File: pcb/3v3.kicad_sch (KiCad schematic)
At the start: 6 parts, among them U3 AP3441SHE-7B

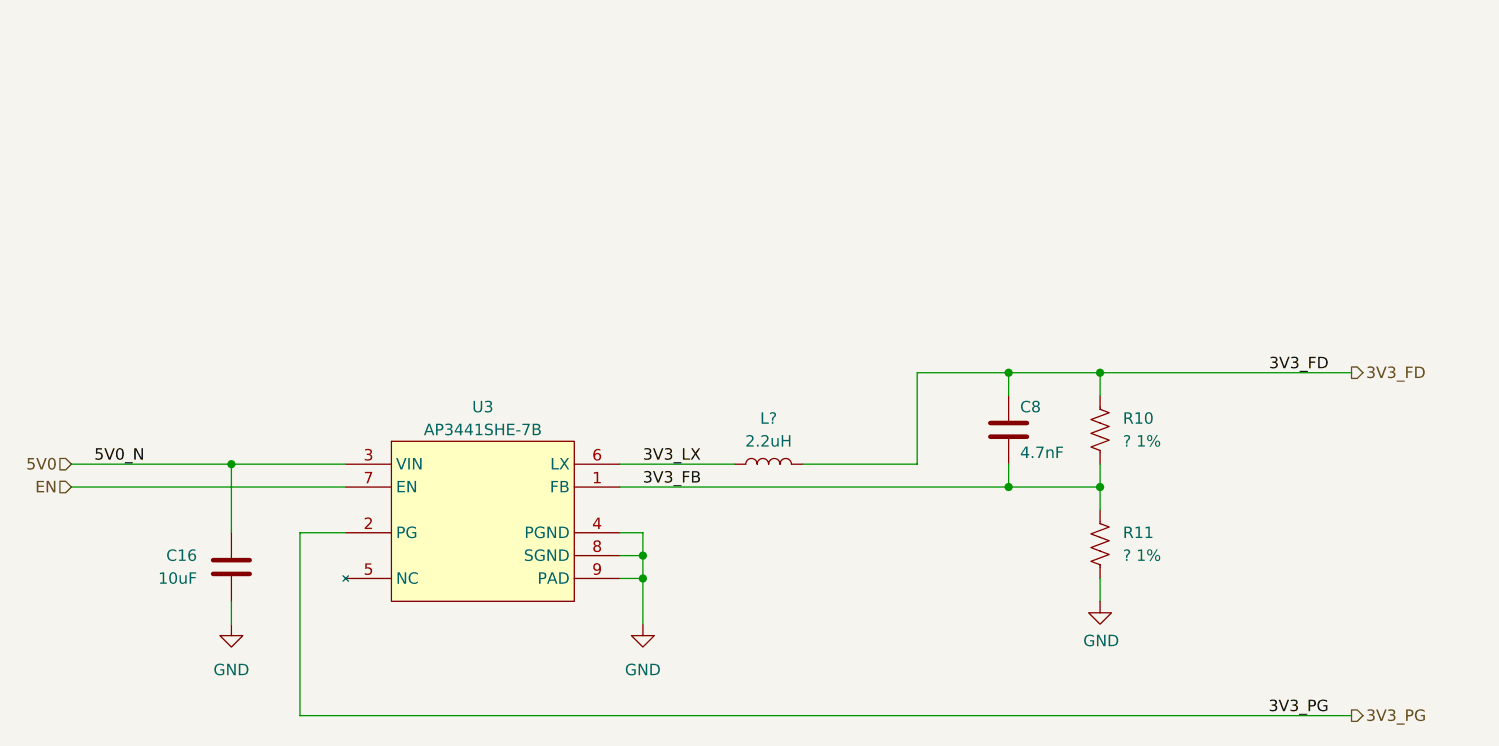
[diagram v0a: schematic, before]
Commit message: changes to power tree
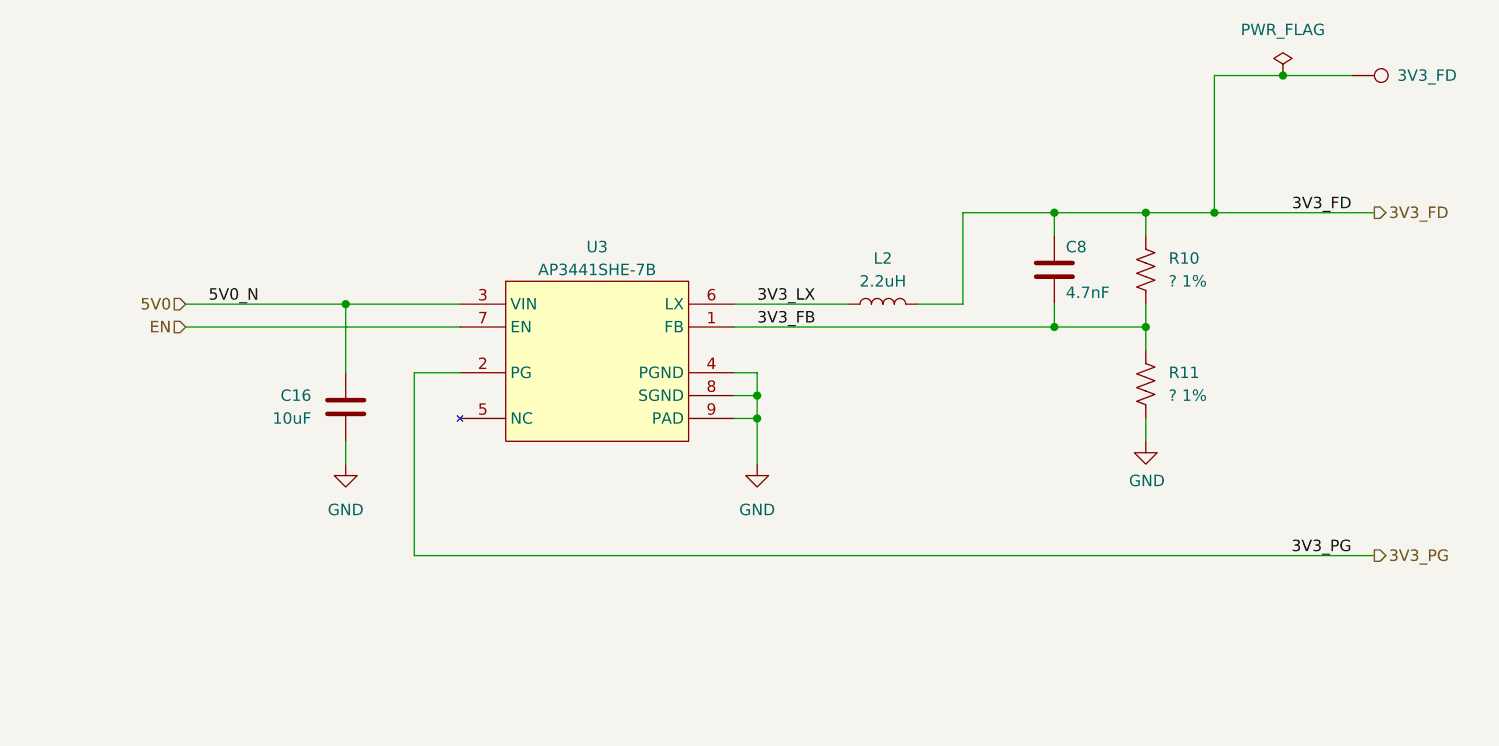
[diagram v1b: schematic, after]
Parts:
- added 3V3_FD: TestPoint, TestPoint:TestPoint_Pad_D1.0mm, symbol library:TestPoint
- gave numbers to parts that had none: 1
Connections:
- net 3V3_FD: now also 3V3_FD.1
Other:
- moved on the sheet: C16, C8, L2, R10, R11, U3

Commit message: moved stuff around, bom
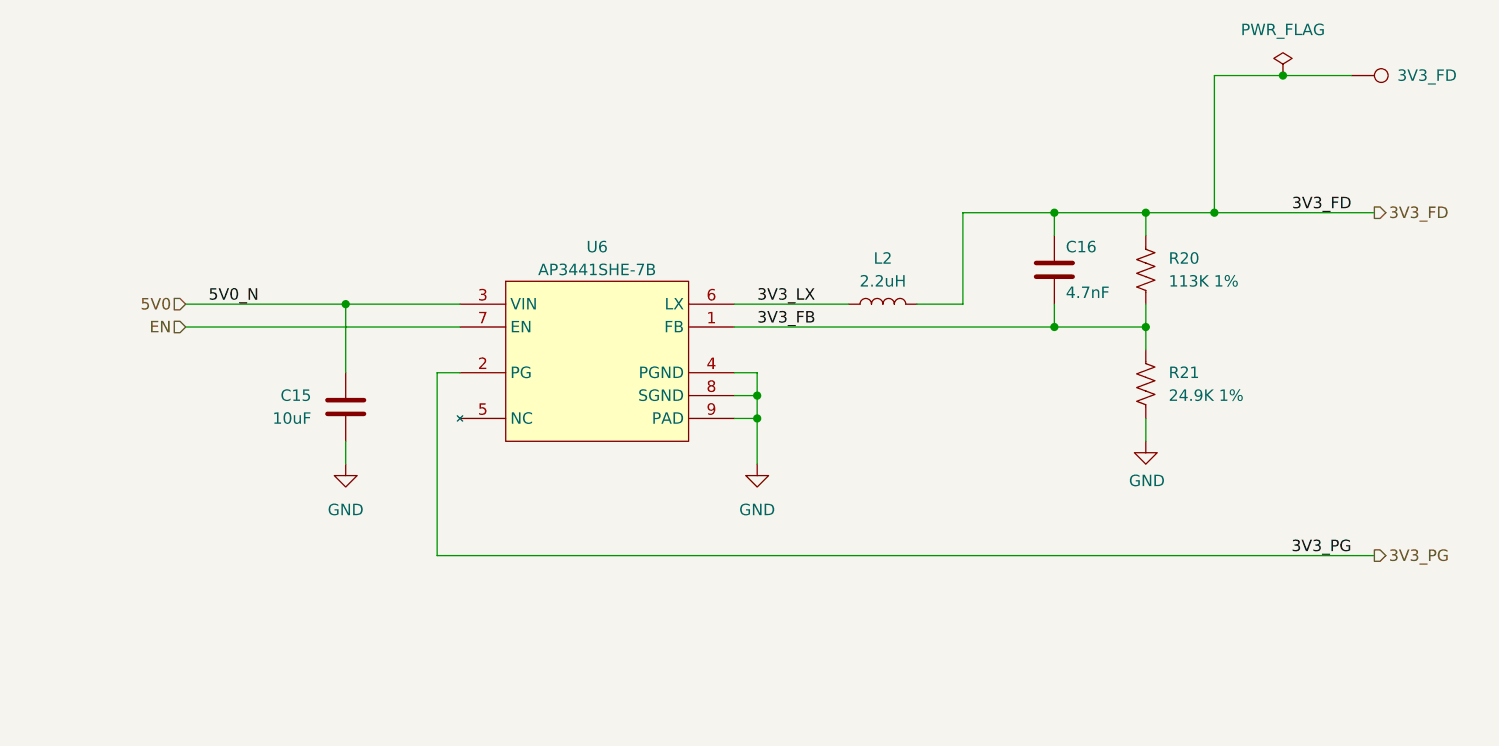
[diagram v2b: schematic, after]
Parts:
- R20: renamed from R10; value ? 1% -> 113K 1%
- R21: renamed from R11; value ? 1% -> 24.9K 1%
- renumbered C16 to C15, C8 to C16, U3 to U6
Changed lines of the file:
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@@
 		(at 93.98 88.9)
 		(diameter 0)
-		(color 0 0 0 0)
+		(color 255 0 0 1)
 	)
 	(junction
@@
 	(wire
 		(pts
-			(xy 101.6 116.84) (xy 208.28 116.84)
+			(xy 104.14 116.84) (xy 208.28 116.84)
 		)
 		(stroke
@@
 	(wire
 		(pts
-			(xy 101.6 96.52) (xy 106.68 96.52)
+			(xy 104.14 96.52) (xy 106.68 96.52)
 		)
 		(stroke
@@
 	(wire
 		(pts
-			(xy 101.6 96.52) (xy 101.6 116.84)
+			(xy 104.14 96.52) (xy 104.14 116.84)
 		)
 		(stroke
@@
 		(on_board yes)
 		(dnp no)
-		(property "Reference" "#PWR011"
+		(property "Reference" "#PWR022"
 			(at 182.88 110.49 0)
 			(effects
@@
 			(project "RPi-HwAB-1"
 				(path "/e63e39d7-6ac0-4ffd-8aa3-1841a4541b55/f9ebb56c-78c7-42ac-bc19-ccbf788f5318/623ac269-424c-4b40-80d6-6e60349ac538"
-					(reference "#PWR011")
+					(reference "#PWR022")
 					(unit 1)
 				)
@@
 		(dnp no)
 		(fields_autoplaced yes)
-		(property "Reference" "U3"
+		(property "Reference" "U6"
 			(at 121.92 82.55 0)
 			(effects
@@
 			(project "RPi-HwAB-1"
 				(path "/e63e39d7-6ac0-4ffd-8aa3-1841a4541b55/f9ebb56c-78c7-42ac-bc19-ccbf788f5318/623ac269-424c-4b40-80d6-6e60349ac538"
-					(reference "U3")
+					(reference "U6")
 					(unit 1)
 				)
@@
 		(dnp no)
 		(fields_autoplaced yes)
-		(property "Reference" "#PWR010"
+		(property "Reference" "#PWR021"
 			(at 139.7 113.03 0)
 			(effects
@@
 			(project "RPi-HwAB-1"
 				(path "/e63e39d7-6ac0-4ffd-8aa3-1841a4541b55/f9ebb56c-78c7-42ac-bc19-ccbf788f5318/623ac269-424c-4b40-80d6-6e60349ac538"
-					(reference "#PWR010")
+					(reference "#PWR021")
 					(unit 1)
 				)
@@
 		(dnp no)
 		(fields_autoplaced yes)
-		(property "Reference" "#PWR041"
+		(property "Reference" "#PWR020"
 			(at 93.98 113.03 0)
 			(effects
@@
 			(project "RPi-HwAB-1"
 				(path "/e63e39d7-6ac0-4ffd-8aa3-1841a4541b55/f9ebb56c-78c7-42ac-bc19-ccbf788f5318/623ac269-424c-4b40-80d6-6e60349ac538"
-					(reference "#PWR041")
+					(reference "#PWR020")
 					(unit 1)
 				)
@@
 		(on_board yes)
 		(dnp no)
-		(property "Reference" "C8"
+		(property "Reference" "C16"
 			(at 173.99 82.55 0)
 			(effects
@@
 			(project "RPi-HwAB-1"
 				(path "/e63e39d7-6ac0-4ffd-8aa3-1841a4541b55/f9ebb56c-78c7-42ac-bc19-ccbf788f5318/623ac269-424c-4b40-80d6-6e60349ac538"
-					(reference "C8")
+					(reference "C16")
 					(unit 1)
 				)
@@
 		(on_board yes)
 		(dnp no)
-		(property "Reference" "R11"
+		(property "Reference" "R21"
 			(at 185.42 96.52 0)
 			(effects
@@
 			)
 		)
-		(property "Value" "? 1%"
+		(property "Value" "24.9K 1%"
 			(at 185.42 99.06 0)
 			(effects
@@
 			(project "RPi-HwAB-1"
 				(path "/e63e39d7-6ac0-4ffd-8aa3-1841a4541b55/f9ebb56c-78c7-42ac-bc19-ccbf788f5318/623ac269-424c-4b40-80d6-6e60349ac538"
-					(reference "R11")
+					(reference "R21")
 					(unit 1)
 				)
@@
 		(on_board yes)
 		(dnp no)
-		(property "Reference" "C16"
+		(property "Reference" "C15"
 			(at 90.17 99.0599 0)
 			(effects
@@
 			(project "RPi-HwAB-1"
 				(path "/e63e39d7-6ac0-4ffd-8aa3-1841a4541b55/f9ebb56c-78c7-42ac-bc19-ccbf788f5318/623ac269-424c-4b40-80d6-6e60349ac538"
-					(reference "C16")
+					(reference "C15")
 					(unit 1)
 				)
@@
 		(on_board yes)
 		(dnp no)
-		(property "Reference" "R10"
+		(property "Reference" "R20"
 			(at 185.42 83.82 0)
 			(effects
@@
 			)
 		)
-		(property "Value" "? 1%"
+		(property "Value" "113K 1%"
 			(at 185.42 86.36 0)
 			(effects
@@
 			(project "RPi-HwAB-1"
 				(path "/e63e39d7-6ac0-4ffd-8aa3-1841a4541b55/f9ebb56c-78c7-42ac-bc19-ccbf788f5318/623ac269-424c-4b40-80d6-6e60349ac538"
-					(reference "R10")
+					(reference "R20")
 					(unit 1)
 				)
@@
 		(dnp no)
 		(fields_autoplaced yes)
-		(property "Reference" "#FLG07"
+		(property "Reference" "#FLG05"
 			(at 198.12 61.595 0)
 			(effects
@@
 			(project "RPi-HwAB-1"
 				(path "/e63e39d7-6ac0-4ffd-8aa3-1841a4541b55/f9ebb56c-78c7-42ac-bc19-ccbf788f5318/623ac269-424c-4b40-80d6-6e60349ac538"
-					(reference "#FLG07")
+					(reference "#FLG05")
 					(unit 1)
 				)

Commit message: bom
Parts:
- 3V3_FD: now left out of the parts list
- C15: footprint (none) -> Capacitor_SMD:C_0402_1005Metric; Manufacturer (none) -> Murata Electronics; Manufacturer Product Number (none) -> GRM155R61A106ME11D; Part Description (none) -> CAP CER 10UF 10V X5R 0402
- C16: Part Description (none) -> CAP CER 0402 4.7NF 50V X7R 5%
- L2: footprint Inductor_SMD:L_Vishay_IHLP-1616 -> Inductor_SMD:L_Bourns_SRP1245A; Manufacturer Vishay Dale -> Bourns Inc.; Manufacturer Product Number IHLP1616BZER1R0M01 -> SRP1265A-2R2M; Part Description (none) -> FIXED IND 2.2UH 22A 4.2 MOHM SMD
- R21: renamed from R20; Manufacturer Product Number CRCW040210K0FKED -> CRCW0402113KFKED; Part Description (none) -> RES 113K OHM 1% 1/16W 0402
- R22: renamed from R21; Manufacturer Product Number CRCW04022K20FKED -> CRCW040224K9FKED; Part Description (none) -> RES 24.9K OHM 1% 1/16W 0402
- U6: Part Description (none) -> IC REG BUCK ADJ 3A UDFN20208
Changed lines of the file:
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@@
+			)
+		)
+		(property "Part Description" "IC REG BUCK ADJ 3A UDFN20208"
+			(at 121.92 96.52 0)
+			(effects
+				(font
+					(size 1.27 1.27)
+				)
+				(hide yes)
 			)
 		)
@@
 			)
 		)
-		(property "Footprint" "Inductor_SMD:L_Vishay_IHLP-1616"
+		(property "Footprint" "Inductor_SMD:L_Bourns_SRP1245A"
 			(at 153.67 88.9 0)
 			(effects
@@
 			)
 		)
-		(property "Datasheet" ""
+		(property "Datasheet" "~"
 			(at 153.67 88.9 0)
 			(effects
@@
 			)
 		)
-		(property "Manufacturer" "Vishay Dale"
+		(property "Manufacturer" "Bourns Inc."
 			(at 153.67 88.9 90)
 			(effects
@@
 			)
 		)
-		(property "Manufacturer Product Number" "IHLP1616BZER1R0M01"
+		(property "Manufacturer Product Number" "SRP1265A-2R2M"
+			(at 153.67 88.9 90)
+			(effects
+				(font
+					(size 1.27 1.27)
+				)
+				(hide yes)
+			)
+		)
+		(property "Part Description" "FIXED IND 2.2UH 22A 4.2 MOHM SMD"
 			(at 153.67 88.9 90)
 			(effects
@@
 		(unit 1)
 		(exclude_from_sim no)
-		(in_bom yes)
+		(in_bom no)
 		(on_board yes)
 		(dnp no)
@@
 		)
 		(property "Description" "test point"
+			(at 205.74 63.5 0)
+			(effects
+				(font
+					(size 1.27 1.27)
+				)
+				(hide yes)
+			)
+		)
+		(property "Name" ""
 			(at 205.74 63.5 0)
 			(effects
@@
 			)
 		)
-		(property "Datasheet" ""
+		(property "Datasheet" "~"
 			(at 172.72 85.09 0)
 			(effects
@@
 		)
 		(property "Manufacturer Product Number" "C0402C472J5RECTU"
+			(at 172.72 85.09 0)
+			(effects
+				(font
+					(size 1.27 1.27)
+				)
+				(hide yes)
+			)
+		)
+		(property "Part Description" "CAP CER 0402 4.7NF 50V X7R 5%"
 			(at 172.72 85.09 0)
 			(effects
@@
 		(on_board yes)
 		(dnp no)
-		(property "Reference" "R21"
+		(property "Reference" "R22"
 			(at 185.42 96.52 0)
 			(effects
@@
 			)
 		)
-		(property "Datasheet" ""
+		(property "Datasheet" "~"
 			(at 182.88 97.79 0)
 			(effects
@@
 			)
 		)
-		(property "Manufacturer Product Number" "CRCW04022K20FKED"
+		(property "Manufacturer Product Number" "CRCW040224K9FKED"
 			(at 182.88 97.79 0)
 			(effects
@@
 			)
 		)
+		(property "Part Description" "RES 24.9K OHM 1% 1/16W 0402"
+			(at 182.88 97.79 0)
+			(effects
+				(font
+					(size 1.27 1.27)
+				)
+				(hide yes)
+			)
+		)
 		(pin "1"
 		)
@@
 			(project "RPi-HwAB-1"
 				(path "/e63e39d7-6ac0-4ffd-8aa3-1841a4541b55/f9ebb56c-78c7-42ac-bc19-ccbf788f5318/623ac269-424c-4b40-80d6-6e60349ac538"
-					(reference "R21")
+					(reference "R22")
 					(unit 1)
 				)
@@
 			)
 		)
-		(property "Footprint" ""
+		(property "Footprint" "Capacitor_SMD:C_0402_1005Metric"
 			(at 94.9452 104.14 0)
 			(effects
@@
 		)
 		(property "Description" "Unpolarized capacitor"
+			(at 93.98 100.33 0)
+			(effects
+				(font
+					(size 1.27 1.27)
+				)
+				(hide yes)
+			)
+		)
+		(property "Manufacturer" "Murata Electronics"
+			(at 93.98 100.33 0)
+			(effects
+				(font
+					(size 1.27 1.27)
+				)
+				(hide yes)
+			)
+		)
+		(property "Manufacturer Product Number" "GRM155R61A106ME11D"
+			(at 93.98 100.33 0)
+			(effects
+				(font
+					(size 1.27 1.27)
+				)
+				(hide yes)
+			)
+		)
+		(property "Part Description" "CAP CER 10UF 10V X5R 0402"
 			(at 93.98 100.33 0)
 			(effects
@@
 		(on_board yes)
 		(dnp no)
-		(property "Reference" "R20"
+		(property "Reference" "R21"
 			(at 185.42 83.82 0)
 			(effects
@@
 			)
 		)
-		(property "Datasheet" ""
+		(property "Datasheet" "~"
 			(at 182.88 85.09 0)
 			(effects
@@
 			)
 		)
-		(property "Manufacturer Product Number" "CRCW040210K0FKED"
+		(property "Manufacturer Product Number" "CRCW0402113KFKED"
 			(at 182.88 85.09 0)
 			(effects
@@
 			)
 		)
+		(property "Part Description" "RES 113K OHM 1% 1/16W 0402"
+			(at 182.88 85.09 0)
+			(effects
+				(font
+					(size 1.27 1.27)
+				)
+				(hide yes)
+			)
+		)
 		(pin "1"
 		)
@@
 			(project "RPi-HwAB-1"
 				(path "/e63e39d7-6ac0-4ffd-8aa3-1841a4541b55/f9ebb56c-78c7-42ac-bc19-ccbf788f5318/623ac269-424c-4b40-80d6-6e60349ac538"
-					(reference "R20")
-					(unit 1)
-				)
+					(reference "R21")
+					(unit 1)
+				)

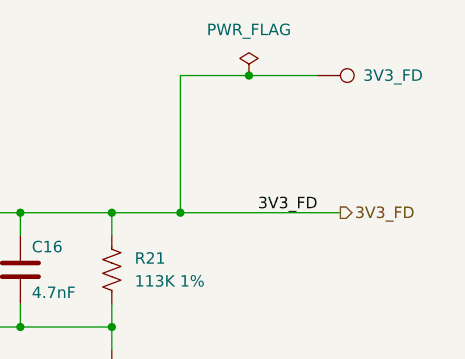
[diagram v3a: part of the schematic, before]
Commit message: initial layout, dogbone fanout
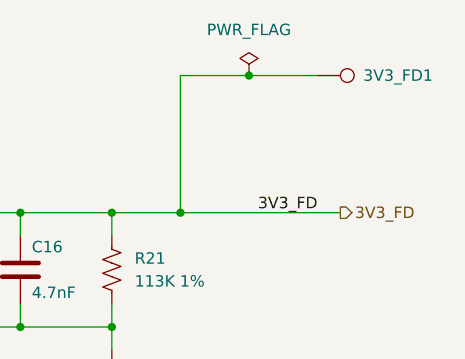
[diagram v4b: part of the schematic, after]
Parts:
- renumbered 3V3_FD to 3V3_FD1
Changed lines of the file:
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@@
 		(on_board yes)
 		(dnp no)
-		(property "Reference" "3V3_FD"
+		(property "Reference" "3V3_FD1"
 			(at 210.82 63.5 90)
 			(effects
@@
 			(project "RPi-HwAB-1"
 				(path "/e63e39d7-6ac0-4ffd-8aa3-1841a4541b55/f9ebb56c-78c7-42ac-bc19-ccbf788f5318/623ac269-424c-4b40-80d6-6e60349ac538"
-					(reference "3V3_FD")
+					(reference "3V3_FD1")
 					(unit 1)
 				)
